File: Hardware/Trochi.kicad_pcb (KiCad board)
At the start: 2 copper layers, 18.5 x 25 mm, 51 parts, among them IC1 ICM-42688-P, J1 JST-SH, J2 JST-SH, J3 JST PH, J6 JST-SH, J7 JST-SH, Q1 AO3400A, Q2 AO3400A, Q3 AO3400A, Q4 AO3400A, Q5 AO3400A, U1 ME6211C33M5, U3 YX-SMD5020

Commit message: feat: complete PCB routing
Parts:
- moved R12 0.98 mm to (140.7, 108.5), turned to 0 degrees
- moved R2 0.13 mm to (140.7, 113.1)
- moved R5 0.11 mm to (142.9, 113.1)
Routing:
- net /VBAT: track 34.2 -> 77.0 mm, vias 0 -> 6
- net SPI_MOSI: track 10.2 -> 23.3 mm, vias 0 -> 1
- net Net-(D2-A): track 0.00 -> 13.1 mm
- net CS_IMU: track 0.00 -> 12.5 mm, vias 0 -> 2
- net +3.3V: track 39.3 -> 51.4 mm, vias 1 -> 4
- net PWM_M1: track 0.00 -> 10.8 mm
- net PWM_M3: track 0.00 -> 10.2 mm
- net Net-(D3-A): track 0.00 -> 9.97 mm, vias 0 -> 2
- net IMU_INT: track 0.00 -> 7.61 mm
- net SPI_SCK: track 13.2 -> 20.7 mm, vias 0 -> 1
- net Net-(Q3-G): track 0.00 -> 7.12 mm
- net SPI_MISO: track 15.3 -> 21.9 mm, vias 0 -> 1
- net GND: track 9.40 -> 15.0 mm, vias 0 -> 3
- net Net-(D1-A): track 0.00 -> 5.37 mm
- net Net-(Q1-G): track 0.00 -> 5.27 mm
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- added copper zone on F.Cu, net GND

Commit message: chore: snapshot PCB state before full re-layout
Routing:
- net GND: track 15.0 -> 28.0 mm, vias 3 -> 6
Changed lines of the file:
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@@
 		(embedded_fonts no)
 		(model "C:/Users/husey/OneDrive/Belgeler/Trochi/Libraries/3D_Models/esp32_s3_supermini.step"
-			(opacity 0.0000)
 			(offset
 				(xyz 0 0 17.5)
@@
 	)
 	(segment
+		(start 139.76 104.33)
+		(end 138.956304 104.33)
+		(width 0.2)
+		(layer "F.Cu")
+		(net "GND")
+	)
+	(segment
+		(start 140.87 105.61)
+		(end 140.32 105.61)
+		(width 0.2)
+		(layer "F.Cu")
+		(net "GND")
+	)
+	(segment
 		(start 142.480947 113.1)
 		(end 143.300947 113.92)
@@
 	)
 	(segment
+		(start 140.87 106.11)
+		(end 140.87 106.61)
+		(width 0.2)
+		(layer "F.Cu")
+		(net "GND")
+	)
+	(segment
+		(start 142.29 105.61)
+		(end 142.02 105.34)
+		(width 0.2)
+		(layer "F.Cu")
+		(net "GND")
+	)
+	(segment
+		(start 143.17 105.61)
+		(end 143.17 106.11)
+		(width 0.2)
+		(layer "F.Cu")
+		(net "GND")
+	)
+	(segment
+		(start 140.32 105.61)
+		(end 140.05 105.34)
+		(width 0.2)
+		(layer "F.Cu")
+		(net "GND")
+	)
+	(segment
 		(start 142.4 113.1)
 		(end 142.480947 113.1)
@@
 	)
 	(segment
+		(start 142.02 104.96)
+		(end 141.52 104.96)
+		(width 0.2)
+		(layer "F.Cu")
+		(net "GND")
+	)
+	(segment
+		(start 140.05 105.34)
+		(end 140.05 104.62)
+		(width 0.2)
+		(layer "F.Cu")
+		(net "GND")
+	)
+	(segment
+		(start 143.17 105.61)
+		(end 142.29 105.61)
+		(width 0.2)
+		(layer "F.Cu")
+		(net "GND")
+	)
+	(segment
+		(start 143.945 102.220865)
+		(end 143.884135 102.16)
+		(width 0.2)
+		(layer "F.Cu")
+		(net "GND")
+	)
+	(segment
+		(start 141.52 105.493583)
+		(end 141.262145 105.751438)
+		(width 0.2)
+		(layer "F.Cu")
+		(net "GND")
+	)
+	(segment
+		(start 140.87 105.61)
+		(end 140.87 106.11)
+		(width 0.2)
+		(layer "F.Cu")
+		(net "GND")
+	)
+	(segment
+		(start 138.956304 104.33)
+		(end 138.475 103.848696)
+		(width 0.2)
+		(layer "F.Cu")
+		(net "GND")
+	)
+	(segment
+		(start 138.475 103.848696)
+		(end 138.475 102.43)
+		(width 0.2)
+		(layer "F.Cu")
+		(net "GND")
+	)
+	(segment
 		(start 138.225 106.11)
 		(end 138.225 107.35)
@@
 	)
 	(segment
+		(start 143.884135 102.16)
+		(end 143.695 102.16)
+		(width 0.2)
+		(layer "F.Cu")
+		(net "GND")
+	)
+	(segment
+		(start 140.05 104.62)
+		(end 139.76 104.33)
+		(width 0.2)
+		(layer "F.Cu")
+		(net "GND")
+	)
+	(segment
 		(start 138.225 107.35)
 		(end 138.675 107.8)
@@
 		(net "GND")
 	)
+	(segment
+		(start 141.52 104.96)
+		(end 141.52 105.493583)
+		(width 0.2)
+		(layer "F.Cu")
+		(net "GND")
+	)
+	(segment
+		(start 142.02 105.34)
+		(end 142.02 104.96)
+		(width 0.2)
+		(layer "F.Cu")
+		(net "GND")
+	)
 	(via
 		(at 138.675 107.8)
@@
 		(net "GND")
 	)
+	(via
+		(at 141.262145 105.751438)
+		(size 0.6)
+		(drill 0.3)
+		(layers "F.Cu" "B.Cu")
+		(net "GND")
+	)
+	(via
+		(at 143.945 102.220865)
+		(size 0.6)
+		(drill 0.3)
+		(layers "F.Cu" "B.Cu")
+		(net "GND")
+	)
+	(via
+		(at 138.475 102.43)
+		(size 0.6)
+		(drill 0.3)
+		(layers "F.Cu" "B.Cu")
+		(net "GND")
+	)
 	(segment
 		(start 140.895 101.19)
@@
 	)
 	(segment
+		(start 138.475 103.092499)
+		(end 138.475 102.43)
+		(width 0.2)
+		(layer "B.Cu")
+		(net "GND")
+	)
+	(segment
 		(start 140.745 106.16)
 		(end 141.245 105.66)
@@
 	)
 	(segment
+		(start 136.225 103.83)
+		(end 136.3125 103.7425)
+		(width 0.2)
+		(layer "B.Cu")
+		(net "GND")
+	)
+	(segment
 		(start 139.9425 103.3925)
 		(end 138.8675 103.3925)
@@
 	)
 	(segment
+		(start 137.824999 103.7425)
+		(end 138.475 103.092499)
+		(width 0.2)
+		(layer "B.Cu")
+		(net "GND")
+	)
+	(segment
 		(start 136.235 103.82)
 		(end 136.225 103.83)
@@
 	)
 	(segment
+		(start 136.3125 103.7425)
+		(end 137.824999 103.7425)
+		(width 0.2)
+		(layer "B.Cu")
+		(net "GND")
+	)
+	(segment
 		(start 138.685 107.8)
 		(end 138.685 108.64)
@@
 		(hatch edge 0.5)
 		(connect_pads
-			(clearance 0.3)
+			(clearance 0.2)
 		)
 		(min_thickness 0.25)

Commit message: feat: Routing Completed :)
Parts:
- removed U2: ~, trochi_footprint:esp32_s3_supermini
- added C14: 10nF, Capacitor_SMD:C_0402_1005Metric, F.Cu at (176.1, 51.6)
- added J4: Conn_01x09, Connector_PinHeader_2.54mm:PinHeader_1x09_P2.54mm_Vertical, F.Cu at (172.5, 42.0)
- added J5: Conn_01x09, Connector_PinHeader_2.54mm:PinHeader_1x09_P2.54mm_Vertical, F.Cu at (187.7, 42.0)
- C11: value 100nF -> 2.2uF
- moved C6 75.6 mm to (185.5, 43.4), turned to 90 degrees
- moved C7 75.5 mm to (185.0, 46.1), turned to -90 degrees
- moved R16 73.4 mm to (185.0, 52.9), turned to 180 degrees
- moved D5 72.8 mm to (184.7, 51.6)
- moved Q5 72.5 mm to (184.2, 55.3), turned to 180 degrees
- moved C8 72.2 mm to (186.0, 46.1)
- moved C9 71.4 mm to (174.7, 42.2), turned to 0 degrees
- moved U1 71.3 mm to (184.2, 48.8), turned to 0 degrees
- moved R17 70.9 mm to (183.0, 52.9), turned to 180 degrees
- moved R11 70.4 mm to (182.6, 51.4)
- moved C10 70.0 mm to (180.2, 48.8)
- moved D6 69.6 mm to (180.8, 51.1)
- moved D3 69.3 mm to (178.5, 47.4), turned to 90 degrees
- moved R5 69.0 mm to (186.0, 59.2), turned to 90 degrees
- moved R6 68.4 mm to (174.7, 43.3), turned to 0 degrees
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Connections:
- C10 pad 1: +3.3V -> GND
- C10 pad 2: GND -> +3.3V
- C11 pad 1: +3.3V -> GND
- C11 pad 2: GND -> +3.3V
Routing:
- net GND: track 28.0 -> 41.2 mm
- net /VBAT: track 77.0 -> 68.4 mm, vias 6 -> 4
- net +3.3V: track 51.4 -> 43.6 mm
- net PWM_M1: track 10.8 -> 3.03 mm
- net PWM_M3: track 10.2 -> 2.84 mm
- net SPI_MISO: track 21.9 -> 15.9 mm, vias 1 -> 0
- net SPI_SCK: track 20.7 -> 26.3 mm, vias 1 -> 2
- net Net-(D6-A): track 11.6 -> 6.70 mm, vias 2 -> 0
- net SPI_MOSI: track 23.3 -> 18.4 mm
- net Net-(D3-A): track 9.97 -> 5.58 mm, vias 2 -> 0
- net Net-(D2-A): track 13.1 -> 9.32 mm
- net Net-(Q3-G): track 7.12 -> 3.92 mm
- net BUZZER_CTRL: track 5.58 -> 2.50 mm, vias 1 -> 0
- net Net-(Q2-G): track 2.47 -> 5.03 mm
- net CS_SD: track 9.59 -> 7.42 mm
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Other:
- board size 18.5 x 25 mm -> 19 x 26.2 mm

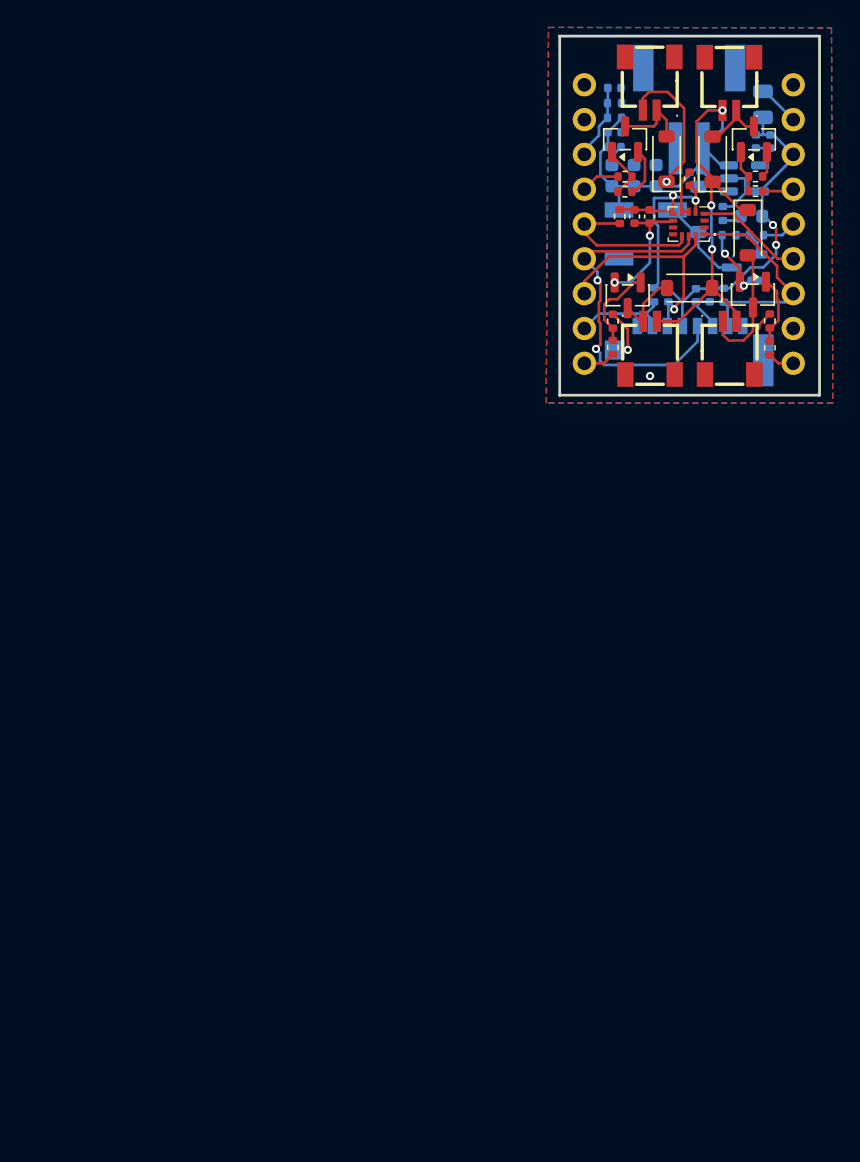
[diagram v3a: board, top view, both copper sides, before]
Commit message: chore: add finishing details to PCB layout
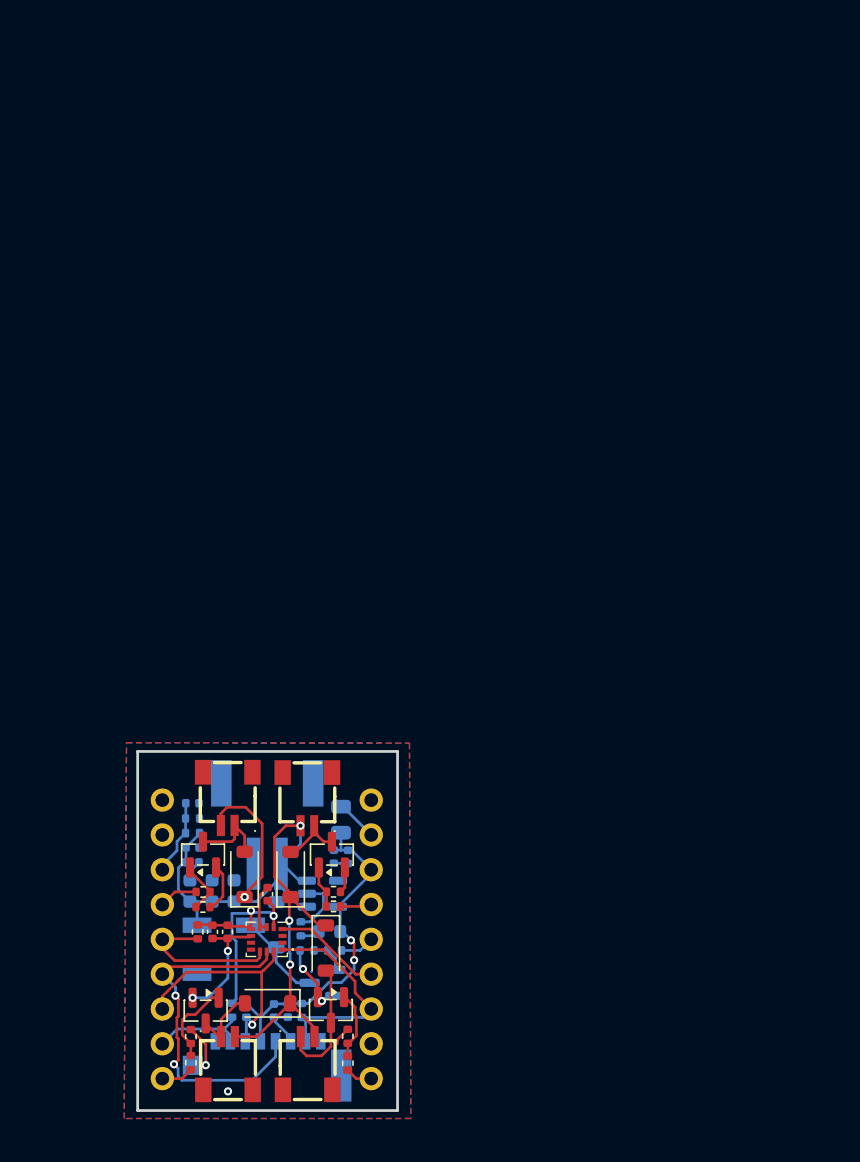
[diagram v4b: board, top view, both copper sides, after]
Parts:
- moved C2 60.6 mm to (143.7, 100.8)
- moved C3 60.6 mm to (145.3, 100.8)
- moved C5 60.6 mm to (143.9, 98.7)
- moved C7 60.6 mm to (154.2, 98.3)
- moved Card1 60.6 mm to (149.3, 113.0)
- moved J2 60.6 mm to (152.3, 113.4)
- moved C11 60.6 mm to (146.4, 103.8)
- moved C9 60.6 mm to (143.9, 94.4)
- moved D5 60.6 mm to (153.9, 103.8)
- moved J1 60.6 mm to (146.5, 113.4)
- moved R11 60.6 mm to (151.8, 103.5)
- moved R13 60.6 mm to (147.8, 109.5)
- moved C1 60.6 mm to (143.9, 97.6)
- moved C12 60.6 mm to (150.8, 109.5)
- moved C4 60.6 mm to (146.9, 100.8)
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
